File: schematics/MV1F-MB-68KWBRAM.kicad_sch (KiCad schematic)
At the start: 8 parts, among them U1 68000

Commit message: complete DaughterBoard
rename sub files
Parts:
- renumbered 1M to 1M?, 2M to 2M?, 6M to 6M?, 7M to 7M?, JP1 to JP?, RN4 to RN?, SP1 to SP?, U1 to U?
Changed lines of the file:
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@@
   (symbol (lib_id "power:GND") (at 158.75 100.33 0) (unit 1)
     (in_bom yes) (on_board yes) (dnp no) (fields_autoplaced)
-    (property "Reference" "#PWR05" (at 158.75 106.68 0)
+    (property "Reference" "#PWR?" (at 158.75 106.68 0)
       (effects (font (size 1.27 1.27)) hide)
     )
@@
       (project "MVS"
         (path "/8d0803ab-15ed-47a7-8dcb-ab27dc5b29c2"
-          (reference "#PWR05") (unit 1)
+          (reference "#PWR?") (unit 1)
         )
         (path "/8d0803ab-15ed-47a7-8dcb-ab27dc5b29c2/0b42d888-4b79-4625-b2d5-9f4b583469ed"
@@
   (symbol (lib_id "Memory_RAM:KM62256CLP") (at 339.09 110.49 0) (unit 1)
     (in_bom yes) (on_board yes) (dnp no)
-    (property "Reference" "6M" (at 331.47 88.9 0)
+    (property "Reference" "6M?" (at 331.47 88.9 0)
       (effects (font (size 1.27 1.27)) (justify right))
     )
@@
       (project "MVS"
         (path "/8d0803ab-15ed-47a7-8dcb-ab27dc5b29c2"
-          (reference "6M") (unit 1)
+          (reference "6M?") (unit 1)
         )
         (path "/8d0803ab-15ed-47a7-8dcb-ab27dc5b29c2/0b42d888-4b79-4625-b2d5-9f4b583469ed"
@@
   (symbol (lib_id "Memory_RAM:KM62256CLP") (at 339.09 58.42 0) (unit 1)
     (in_bom yes) (on_board yes) (dnp no)
-    (property "Reference" "7M" (at 331.47 36.83 0)
+    (property "Reference" "7M?" (at 331.47 36.83 0)
       (effects (font (size 1.27 1.27)) (justify right))
     )
@@
       (project "MVS"
         (path "/8d0803ab-15ed-47a7-8dcb-ab27dc5b29c2"
-          (reference "7M") (unit 1)
+          (reference "7M?") (unit 1)
         )
         (path "/8d0803ab-15ed-47a7-8dcb-ab27dc5b29c2/0b42d888-4b79-4625-b2d5-9f4b583469ed"
@@
   (symbol (lib_id "0-Custom-cbm-steve:27C1024") (at 176.53 59.69 0) (unit 1)
     (in_bom yes) (on_board yes) (dnp no)
-    (property "Reference" "SP1" (at 167.64 34.29 0)
+    (property "Reference" "SP?" (at 167.64 34.29 0)
       (effects (font (size 1.27 1.27)))
     )
@@
       (project "MVS"
         (path "/8d0803ab-15ed-47a7-8dcb-ab27dc5b29c2"
-          (reference "SP1") (unit 1)
+          (reference "SP?") (unit 1)
         )
         (path "/8d0803ab-15ed-47a7-8dcb-ab27dc5b29c2/0b42d888-4b79-4625-b2d5-9f4b583469ed"
@@
   (symbol (lib_id "Device:R_Network04") (at 36.83 45.72 0) (unit 1)
     (in_bom yes) (on_board yes) (dnp no)
-    (property "Reference" "RN4" (at 41.402 44.7619 0)
+    (property "Reference" "RN?" (at 41.402 44.7619 0)
       (effects (font (size 1.27 1.27)) (justify left) hide)
     )
@@
       (project "MVS"
         (path "/8d0803ab-15ed-47a7-8dcb-ab27dc5b29c2"
-          (reference "RN4") (unit 1)
+          (reference "RN?") (unit 1)
         )
         (path "/8d0803ab-15ed-47a7-8dcb-ab27dc5b29c2/0b42d888-4b79-4625-b2d5-9f4b583469ed"
@@
   (symbol (lib_id "power:GND") (at 311.15 142.24 0) (unit 1)
     (in_bom yes) (on_board yes) (dnp no) (fields_autoplaced)
-    (property "Reference" "#PWR09" (at 311.15 148.59 0)
+    (property "Reference" "#PWR?" (at 311.15 148.59 0)
       (effects (font (size 1.27 1.27)) hide)
     )
@@
       (project "MVS"
         (path "/8d0803ab-15ed-47a7-8dcb-ab27dc5b29c2"
-          (reference "#PWR09") (unit 1)
+          (reference "#PWR?") (unit 1)
         )
         (path "/8d0803ab-15ed-47a7-8dcb-ab27dc5b29c2/0b42d888-4b79-4625-b2d5-9f4b583469ed"
@@
   (symbol (lib_id "power:VCC") (at 287.02 30.48 0) (unit 1)
     (in_bom yes) (on_board yes) (dnp no) (fields_autoplaced)
-    (property "Reference" "#PWR08" (at 287.02 34.29 0)
+    (property "Reference" "#PWR?" (at 287.02 34.29 0)
       (effects (font (size 1.27 1.27)) hide)
     )
@@
       (project "MVS"
         (path "/8d0803ab-15ed-47a7-8dcb-ab27dc5b29c2"
-          (reference "#PWR08") (unit 1)
+          (reference "#PWR?") (unit 1)
         )
         (path "/8d0803ab-15ed-47a7-8dcb-ab27dc5b29c2/0b42d888-4b79-4625-b2d5-9f4b583469ed"
@@
   (symbol (lib_id "power:GND") (at 224.79 142.24 0) (unit 1)
     (in_bom yes) (on_board yes) (dnp no) (fields_autoplaced)
-    (property "Reference" "#PWR07" (at 224.79 148.59 0)
+    (property "Reference" "#PWR?" (at 224.79 148.59 0)
       (effects (font (size 1.27 1.27)) hide)
     )
@@
       (project "MVS"
         (path "/8d0803ab-15ed-47a7-8dcb-ab27dc5b29c2"
-          (reference "#PWR07") (unit 1)
+          (reference "#PWR?") (unit 1)
         )
         (path "/8d0803ab-15ed-47a7-8dcb-ab27dc5b29c2/0b42d888-4b79-4625-b2d5-9f4b583469ed"
@@
   (symbol (lib_id "Memory_RAM:KM62256CLP") (at 256.54 58.42 0) (unit 1)
     (in_bom yes) (on_board yes) (dnp no)
-    (property "Reference" "1M" (at 248.92 36.83 0)
+    (property "Reference" "1M?" (at 248.92 36.83 0)
       (effects (font (size 1.27 1.27)) (justify right))
     )
@@
       (project "MVS"
         (path "/8d0803ab-15ed-47a7-8dcb-ab27dc5b29c2"
-          (reference "1M") (unit 1)
+          (reference "1M?") (unit 1)
         )
         (path "/8d0803ab-15ed-47a7-8dcb-ab27dc5b29c2/0b42d888-4b79-4625-b2d5-9f4b583469ed"
@@
   (symbol (lib_id "CPU_NXP_68000:68000D") (at 88.9 92.71 0) (unit 1)
     (in_bom yes) (on_board yes) (dnp no)
-    (property "Reference" "U1" (at 72.39 34.29 0)
+    (property "Reference" "U?" (at 72.39 34.29 0)
       (effects (font (size 1.27 1.27)) (justify left))
     )
@@
       (project "MVS"
         (path "/8d0803ab-15ed-47a7-8dcb-ab27dc5b29c2"
-          (reference "U1") (unit 1)
+          (reference "U?") (unit 1)
         )
         (path "/8d0803ab-15ed-47a7-8dcb-ab27dc5b29c2/0b42d888-4b79-4625-b2d5-9f4b583469ed"
@@
   (symbol (lib_id "Jumper:SolderJumper_2_Open") (at 29.21 107.95 0) (unit 1)
     (in_bom yes) (on_board yes) (dnp no) (fields_autoplaced)
-    (property "Reference" "JP1" (at 29.21 102.9167 0)
+    (property "Reference" "JP?" (at 29.21 102.9167 0)
       (effects (font (size 1.27 1.27)))
     )
@@
       (project "MVS"
         (path "/8d0803ab-15ed-47a7-8dcb-ab27dc5b29c2"
-          (reference "JP1") (unit 1)
+          (reference "JP?") (unit 1)
         )
         (path "/8d0803ab-15ed-47a7-8dcb-ab27dc5b29c2/0b42d888-4b79-4625-b2d5-9f4b583469ed"
@@
   (symbol (lib_id "Memory_RAM:KM62256CLP") (at 256.54 110.49 0) (unit 1)
     (in_bom yes) (on_board yes) (dnp no)
-    (property "Reference" "2M" (at 248.92 88.9 0)
+    (property "Reference" "2M?" (at 248.92 88.9 0)
       (effects (font (size 1.27 1.27)) (justify right))
     )
@@
       (project "MVS"
         (path "/8d0803ab-15ed-47a7-8dcb-ab27dc5b29c2"
-          (reference "2M") (unit 1)
+          (reference "2M?") (unit 1)
         )
         (path "/8d0803ab-15ed-47a7-8dcb-ab27dc5b29c2/0b42d888-4b79-4625-b2d5-9f4b583469ed"
@@
   (symbol (lib_id "power:VCC") (at 90.17 30.48 0) (unit 1)
     (in_bom yes) (on_board yes) (dnp no) (fields_autoplaced)
-    (property "Reference" "#PWR01" (at 90.17 34.29 0)
+    (property "Reference" "#PWR?" (at 90.17 34.29 0)
       (effects (font (size 1.27 1.27)) hide)
     )
@@
       (project "MVS"
         (path "/8d0803ab-15ed-47a7-8dcb-ab27dc5b29c2"
-          (reference "#PWR01") (unit 1)
+          (reference "#PWR?") (unit 1)
         )
         (path "/8d0803ab-15ed-47a7-8dcb-ab27dc5b29c2/0b42d888-4b79-4625-b2d5-9f4b583469ed"
@@
   (symbol (lib_id "power:GND") (at 90.17 156.21 0) (unit 1)
     (in_bom yes) (on_board yes) (dnp no) (fields_autoplaced)
-    (property "Reference" "#PWR02" (at 90.17 162.56 0)
+    (property "Reference" "#PWR?" (at 90.17 162.56 0)
       (effects (font (size 1.27 1.27)) hide)
     )
@@
       (project "MVS"
         (path "/8d0803ab-15ed-47a7-8dcb-ab27dc5b29c2"
-          (reference "#PWR02") (unit 1)
+          (reference "#PWR?") (unit 1)
         )
         (path "/8d0803ab-15ed-47a7-8dcb-ab27dc5b29c2/0b42d888-4b79-4625-b2d5-9f4b583469ed"
@@
   (symbol (lib_id "power:VCC") (at 31.75 36.83 0) (unit 1)
     (in_bom yes) (on_board yes) (dnp no) (fields_autoplaced)
-    (property "Reference" "#PWR03" (at 31.75 40.64 0)
+    (property "Reference" "#PWR?" (at 31.75 40.64 0)
       (effects (font (size 1.27 1.27)) hide)
     )
@@
       (project "MVS"
         (path "/8d0803ab-15ed-47a7-8dcb-ab27dc5b29c2"
-          (reference "#PWR03") (unit 1)
+          (reference "#PWR?") (unit 1)
         )
         (path "/8d0803ab-15ed-47a7-8dcb-ab27dc5b29c2/0b42d888-4b79-4625-b2d5-9f4b583469ed"
@@
   (symbol (lib_id "power:VCC") (at 199.39 29.21 0) (unit 1)
     (in_bom yes) (on_board yes) (dnp no) (fields_autoplaced)
-    (property "Reference" "#PWR06" (at 199.39 33.02 0)
+    (property "Reference" "#PWR?" (at 199.39 33.02 0)
       (effects (font (size 1.27 1.27)) hide)
     )
@@
       (project "MVS"
         (path "/8d0803ab-15ed-47a7-8dcb-ab27dc5b29c2"
-          (reference "#PWR06") (unit 1)
+          (reference "#PWR?") (unit 1)
         )
         (path "/8d0803ab-15ed-47a7-8dcb-ab27dc5b29c2/0b42d888-4b79-4625-b2d5-9f4b583469ed"
@@
   (symbol (lib_id "power:GND") (at 21.59 111.76 0) (unit 1)
     (in_bom yes) (on_board yes) (dnp no) (fields_autoplaced)
-    (property "Reference" "#PWR04" (at 21.59 118.11 0)
+    (property "Reference" "#PWR?" (at 21.59 118.11 0)
       (effects (font (size 1.27 1.27)) hide)
     )
@@
       (project "MVS"
         (path "/8d0803ab-15ed-47a7-8dcb-ab27dc5b29c2"
-          (reference "#PWR04") (unit 1)
-        )
-        (path "/8d0803ab-15ed-47a7-8dcb-ab27dc5b29c2/0b42d888-4b79-4625-b2d5-9f4b583469ed"
+          (reference "#PWR?") (unit 1)
+        )
+        (path "/8d0803ab-15ed-47a7-8dcb-ab27dc5b29c2/0b42d888-4b79-4625-b2d5-9f4b583469ed"

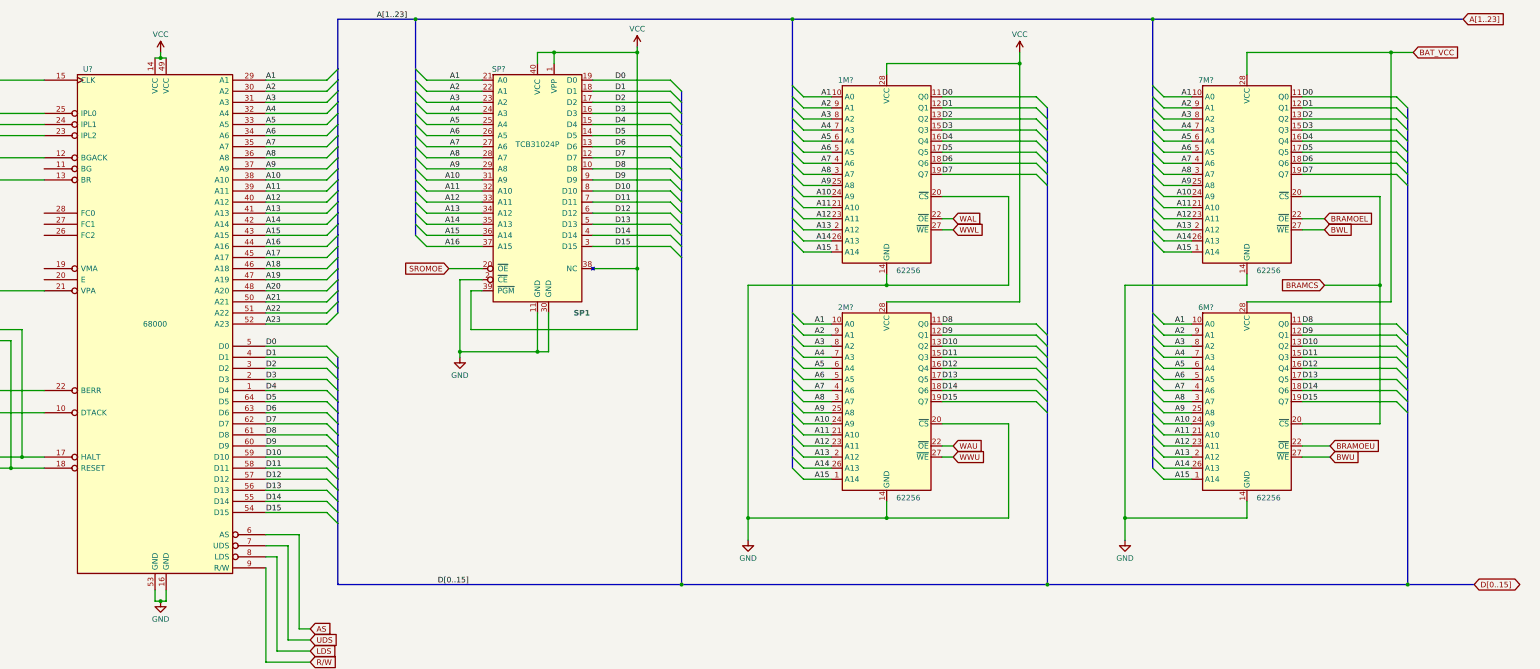
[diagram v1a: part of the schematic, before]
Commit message: Typo... and orphan labels remove
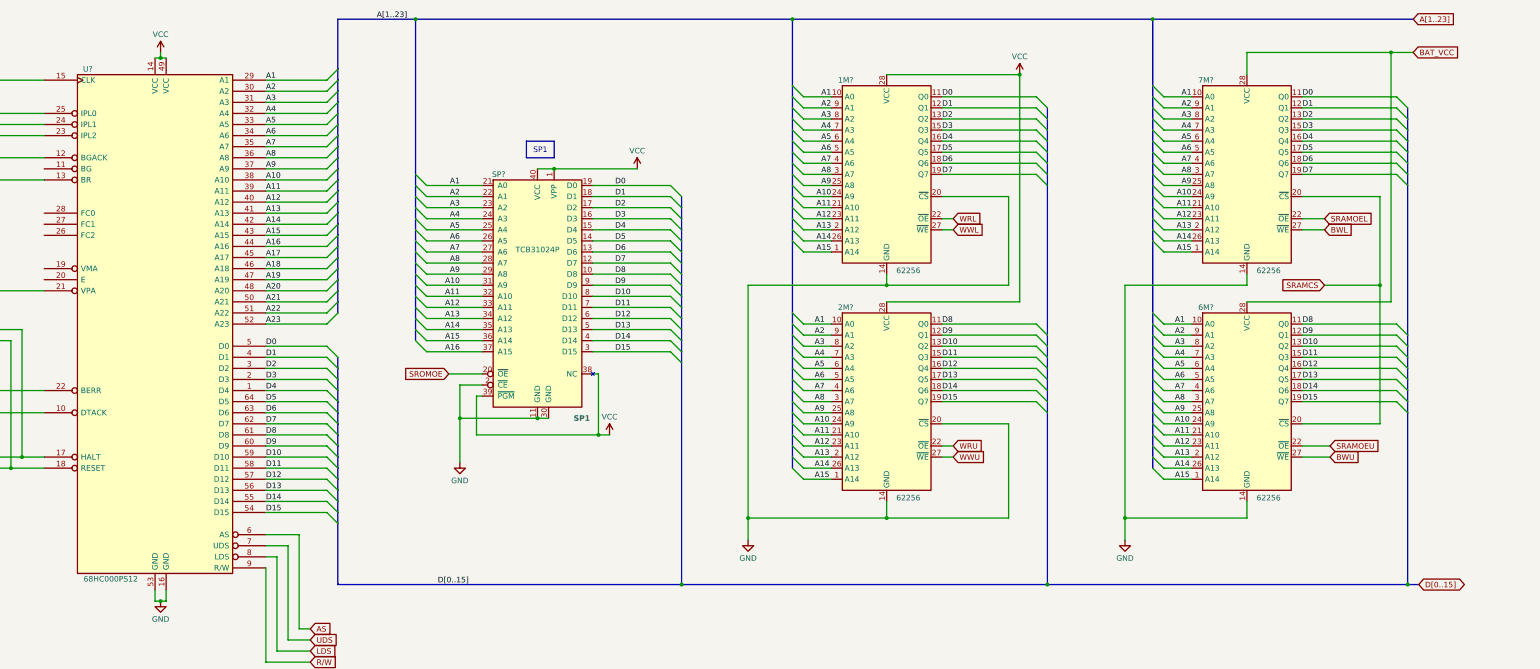
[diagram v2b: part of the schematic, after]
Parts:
- U?: value 68000 -> 68HC000PS12
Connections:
- net BRAMCS renamed SRAMCS
- net BRAMOEL renamed SRAMOEL
- net BRAMOEU renamed SRAMOEU
- net WAL renamed WRL
- net WAU renamed WRU
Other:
- moved on the sheet: SP?

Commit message: Typo
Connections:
- net SRAMCS renamed BRAMCS
- net SRAMOEL renamed BRAMOEL
- net SRAMOEU renamed BRAMOEU
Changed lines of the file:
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@@
     )
   )
-  (global_label "SRAMCS" (shape input) (at 356.87 83.82 180) (fields_autoplaced)
+  (global_label "BRAMCS" (shape input) (at 356.87 83.82 180) (fields_autoplaced)
     (effects (font (size 1.27 1.27)) (justify right))
     (property "Intersheetrefs" "${INTERSHEET_REFS}" (at 346.3253 83.82 0)
@@
     )
   )
-  (global_label "SRAMOEL" (shape input) (at 356.87 68.58 0) (fields_autoplaced)
+  (global_label "BRAMOEL" (shape input) (at 356.87 68.58 0) (fields_autoplaced)
     (effects (font (size 1.27 1.27)) (justify left))
     (property "Intersheetrefs" "${INTERSHEET_REFS}" (at 368.4428 68.58 0)
@@
     )
   )
-  (global_label "SRAMOEU" (shape input) (at 358.14 120.65 0) (fields_autoplaced)
+  (global_label "BRAMOEU" (shape input) (at 358.14 120.65 0) (fields_autoplaced)
     (effects (font (size 1.27 1.27)) (justify left))
     (property "Intersheetrefs" "${INTERSHEET_REFS}" (at 370.0152 120.65 0)
